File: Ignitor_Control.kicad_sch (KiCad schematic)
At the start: 12 parts, among them J20 Ignitor Screw Terminal, K2 G5Q-1A DC24, Q8 BSS138, U8 INA187A1

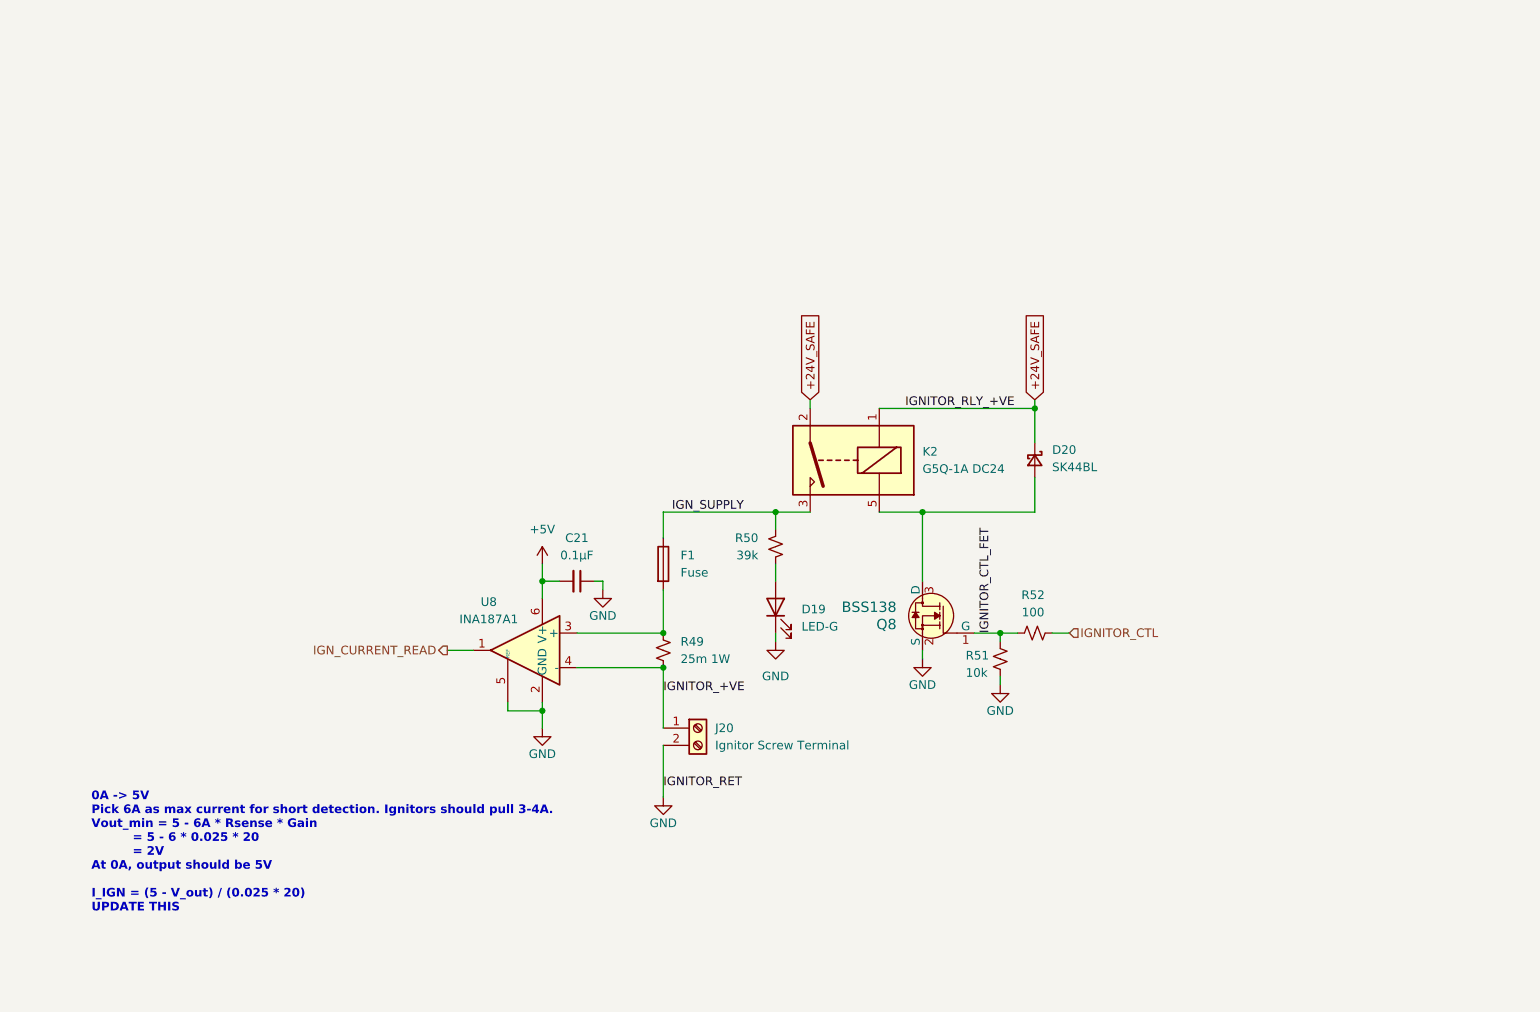
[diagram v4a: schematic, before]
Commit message: add 2 stage lockout to ignitor, add ignitor resistance reading with adc current source
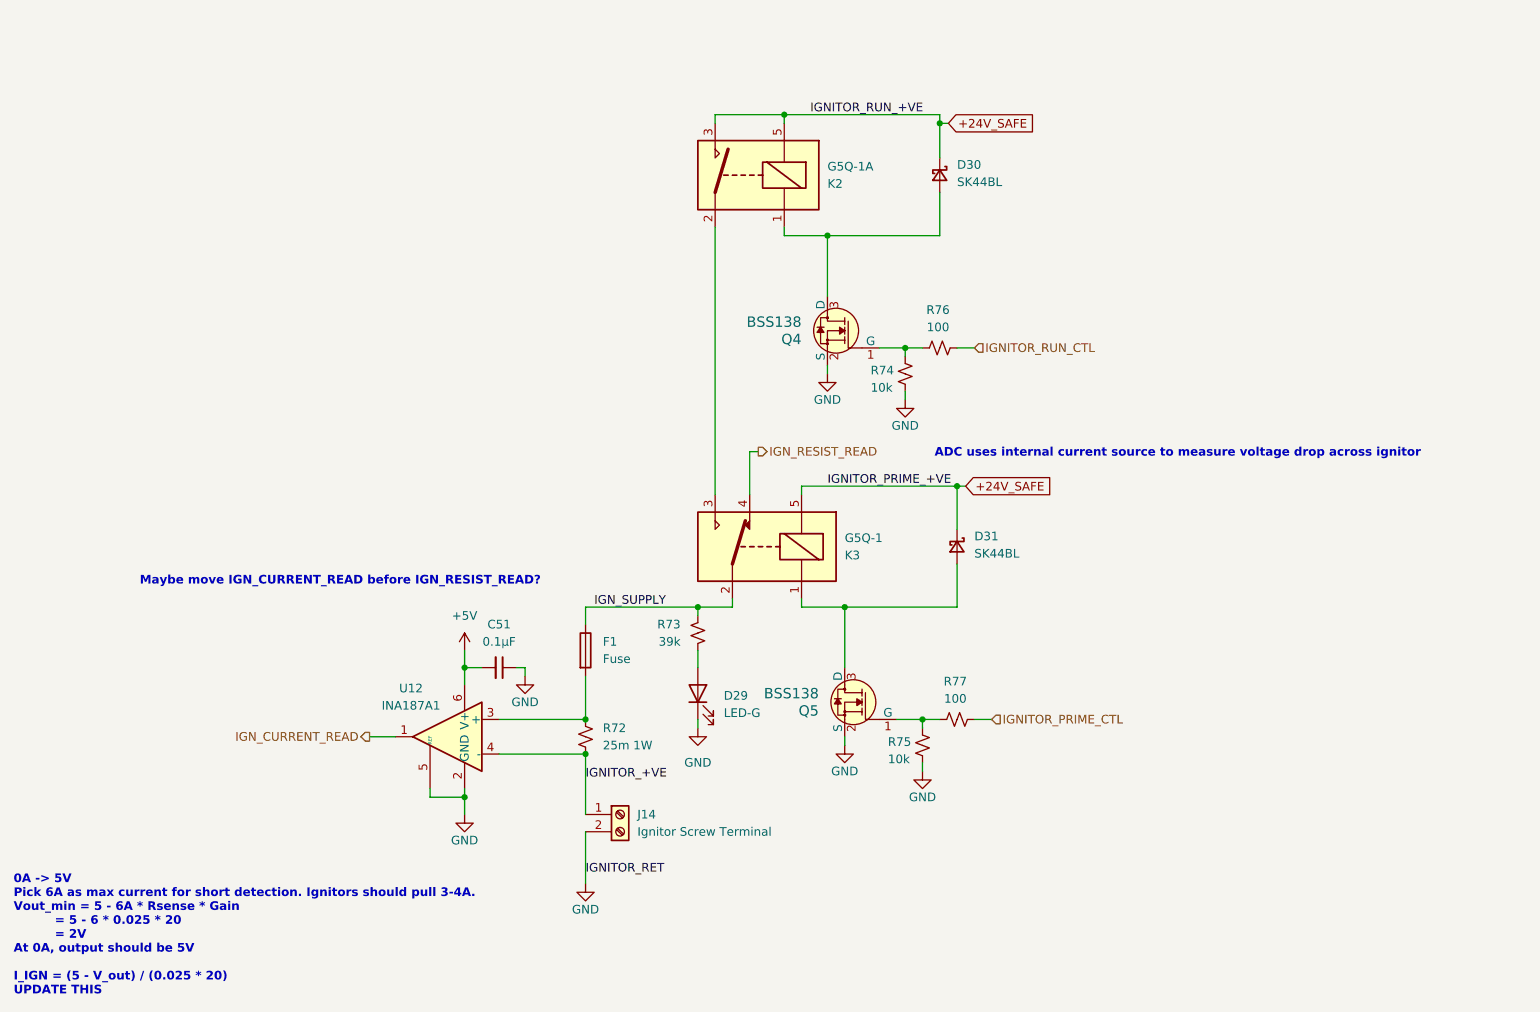
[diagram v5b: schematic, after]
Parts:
- added D30: SK44BL, Diode_SMD:D_SMB, symbol Device:D_Schottky_Small
- added K3: G5Q-1, Relay_THT:Relay_SPDT_Omron-G5Q-1, symbol Relay:G5Q-1
- added Q4: BSS138, Package_TO_SOT_SMD:SOT-23-3, symbol dk_Transistors-FETs-MOSFETs-Single:BSS138
- added R74: 10k, Resistor_SMD:R_0402_1005Metric, symbol Device:R_Small_US
- added R76: 100, Resistor_SMD:R_0402_1005Metric, symbol Device:R_Small_US
- K2: value G5Q-1A DC24 -> G5Q-1A
- renumbered C21 to C51, D19 to D29, D20 to D31, J20 to J14, Q8 to Q5, R49 to R72, R50 to R73, R51 to R75, R52 to R77, U8 to U12
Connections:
- net +24V_SAFE: now also K2.3, K2.5, D30.1 (K), K3.5; no longer K2.1, K2.2
- net GND: now also Q4.2 (S), R74.2
- net IGN_SUPPLY: now also K3.2; no longer K2.3
- net at D31.2 (A), Q5.3 (D): now also K3.1; no longer K2.5
- net IGNITOR_CTL renamed IGNITOR_PRIME_CTL
- net IGNITOR_CTL_FET: no longer names the net of Q5.1 (G), R75.1, R77.1
- new net: D30.2 (A), K2.1, Q4.3 (D)
- new net: K2.2, K3.3
- new net: Q4.1 (G), R74.1, R76.1
- new net IGNITOR_RUN_CTL: R76.2
- new net IGN_RESIST_READ: K3.4
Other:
- note added: "ADC uses internal current source to measure voltage drop across ignitor"
- note added: "Maybe move IGN_CURRENT_READ before IGN_RESIST_READ?"
- moved on the sheet: C51, D29, D31, F1, J14, Q5, R72, R73, R75, R77, U12

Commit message: fix ignitor resistance read circuit to use correct PGA reference
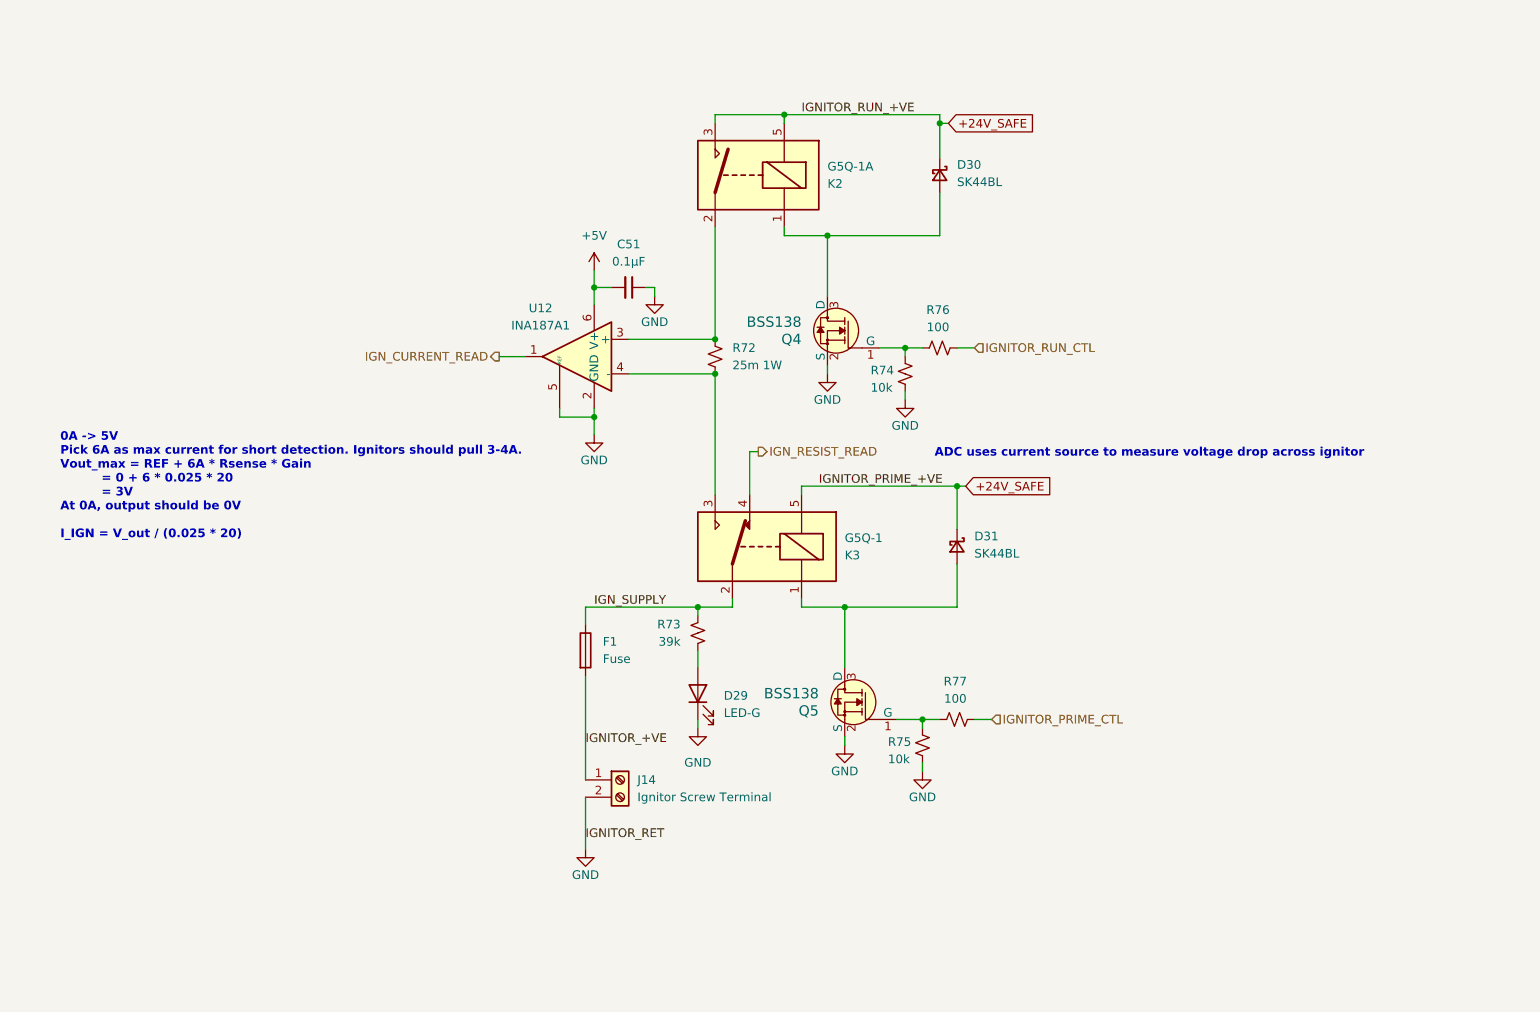
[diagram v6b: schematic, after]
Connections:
- net IGNITOR_+VE: now also F1.2; no longer R72.2, U12.4 (-)
- net at K2.2: now also R72.1, U12.3 (+); no longer K3.3
- new net: K3.3, R72.2, U12.4 (-)
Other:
- note added: "0A -> 5V Pick 6A as max current for short detection. Ignitors should pull 3-4A. Vout_max = REF + 6A * Rsense * Gain = 0 + 6 * 0.025 * 20 = 3V At 0A, output should be 0V I_IGN = V_out / (0.025 * 20)"
- note added: "ADC uses current source to measure voltage drop across ignitor"
- note removed: "0A -> 5V Pick 6A as max current for short detection. Ignitors should pull 3-4A. Vout_min = 5 - 6A * Rsense * Gain = 5 - 6 * 0.025 * 20 = 2V At 0A, output should be 5V I_IGN = (5 - V_out) / (0.025 * 20) UPDATE THIS"
- note removed: "ADC uses internal current source to measure voltage drop across ignitor"
- note removed: "Maybe move IGN_CURRENT_READ before IGN_RESIST_READ?"
- moved on the sheet: C51, J14, R72, U12

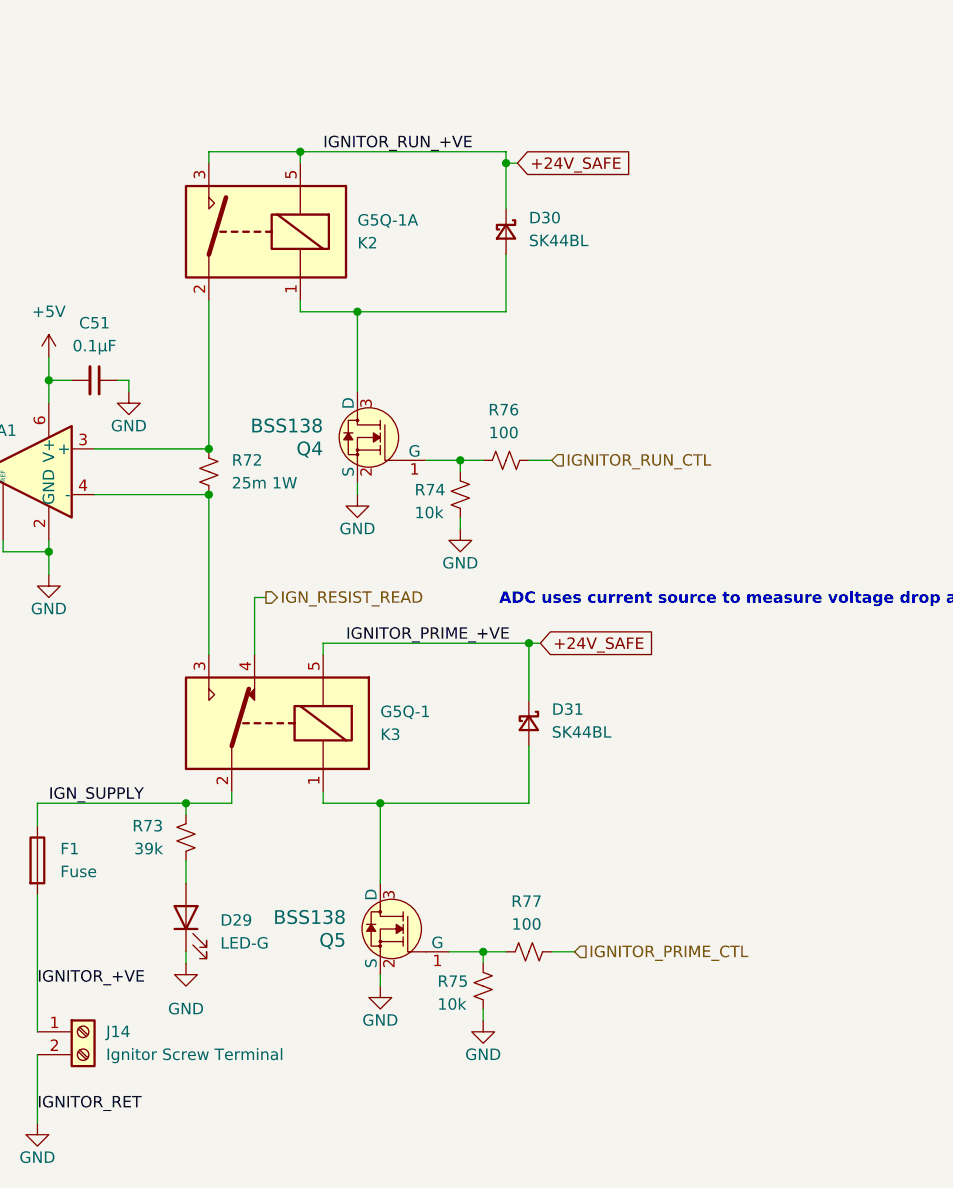
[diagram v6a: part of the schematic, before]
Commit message: ground floating trace between ign relays when relays open
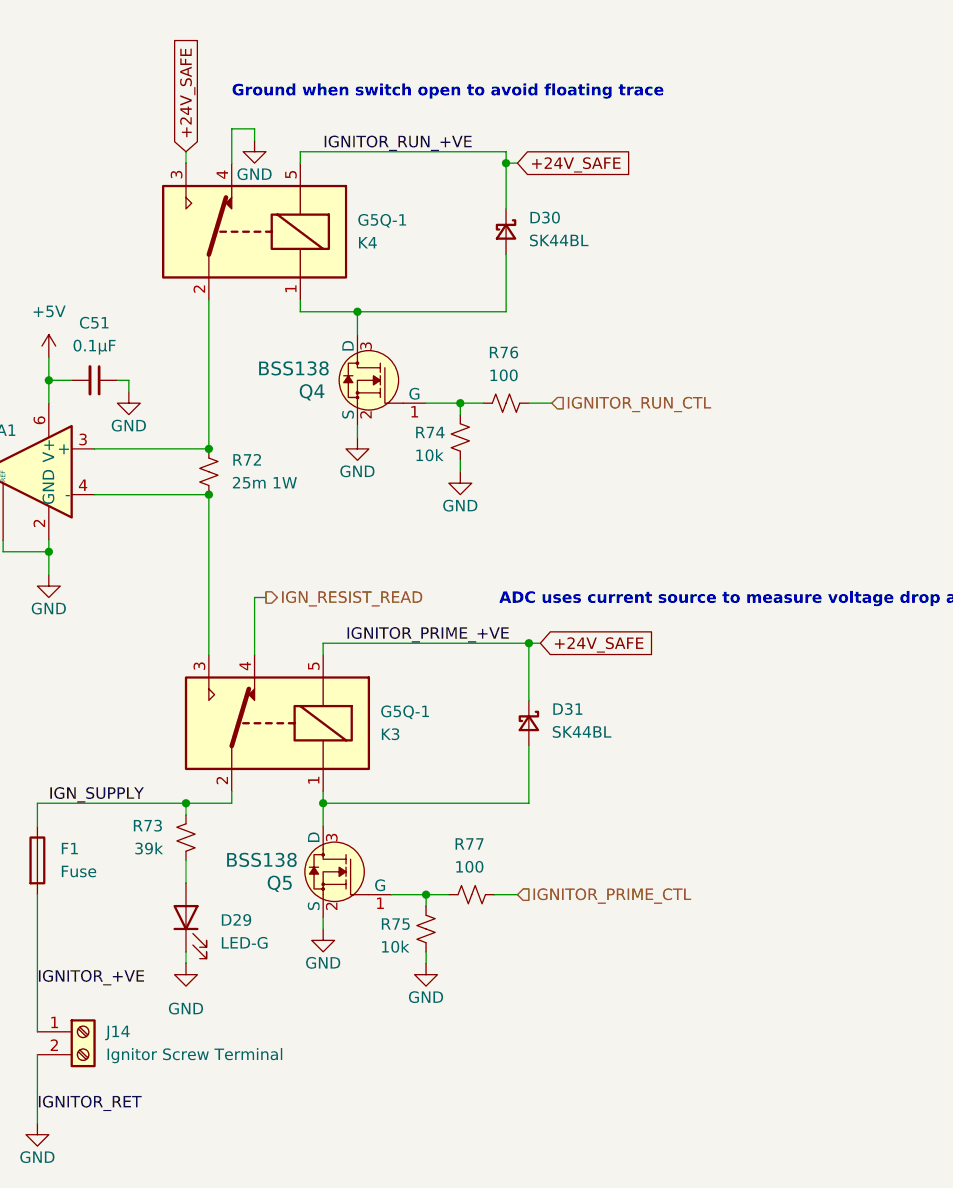
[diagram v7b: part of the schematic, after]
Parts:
- removed K2: G5Q-1A, Relay_THT:Relay_SPST_Omron-G5Q-1A, symbol Relay:G5Q-1A
- added K4: G5Q-1, Relay_THT:Relay_SPDT_Omron-G5Q-1, symbol Relay:G5Q-1
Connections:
- net +24V_SAFE: now also K4.3, K4.5
- net GND: now also K4.4
- net at D30.2 (A), Q4.3 (D): now also K4.1
- net at R72.1, U12.3 (+): now also K4.2
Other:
- note added: "Ground when switch open to avoid floating trace"
- moved on the sheet: Q4, Q5, R74, R75, R76, R77
